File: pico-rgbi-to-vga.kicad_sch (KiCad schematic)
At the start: 25 parts, among them J1 SDS-80J, J2 DB15_Female_HighDensity, J3 USB-B1HSB6, SW1 SW_Push, U1 Pico

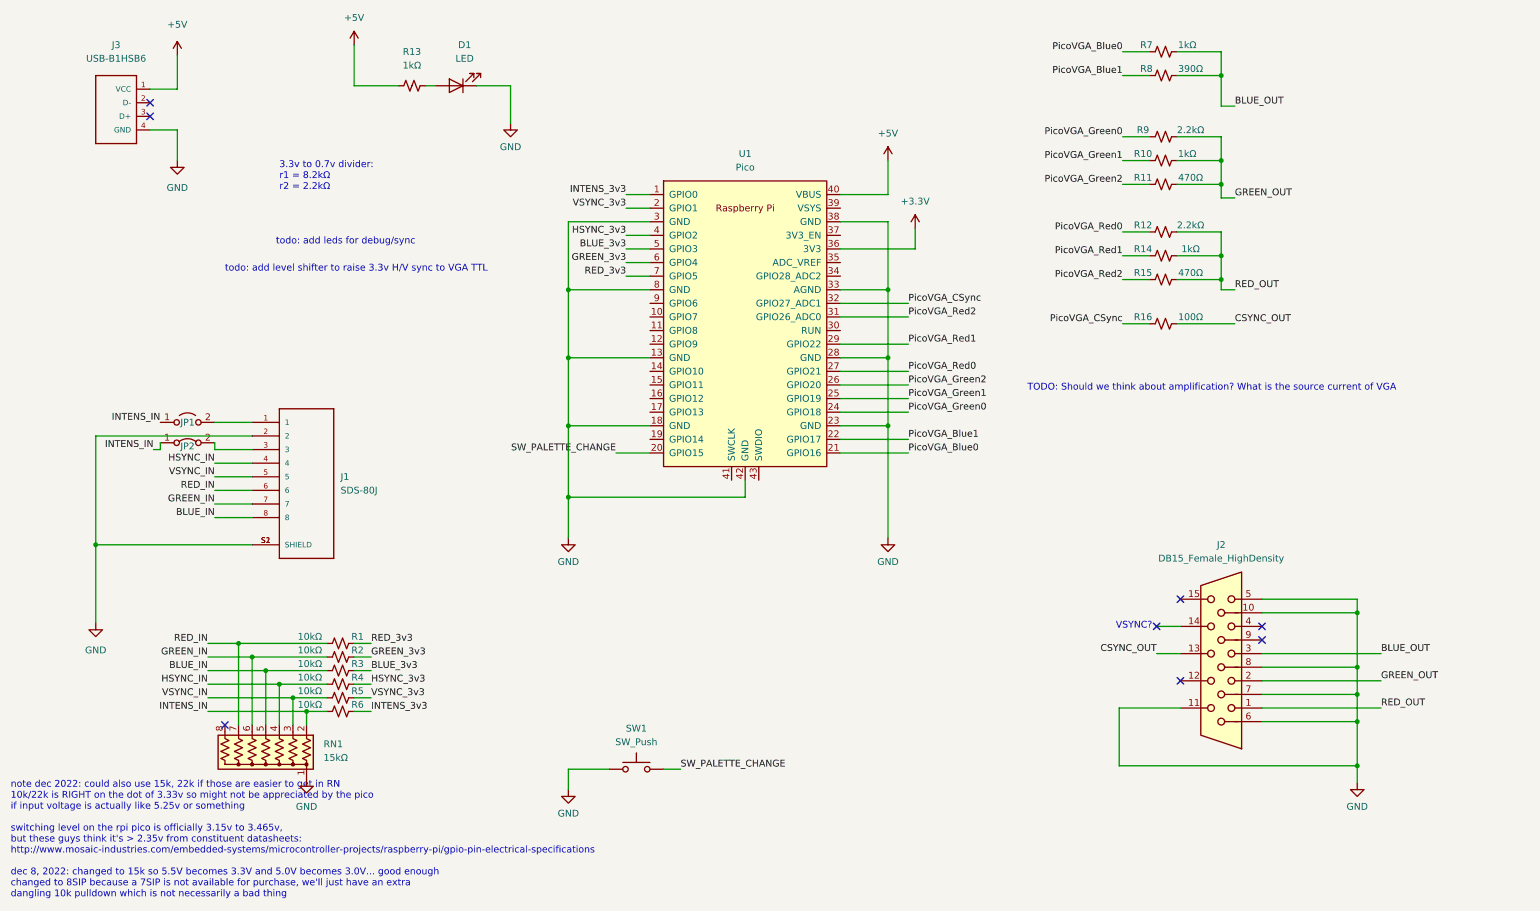
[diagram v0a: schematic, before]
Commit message: Fix VGA output pins to use GPIOs that exist
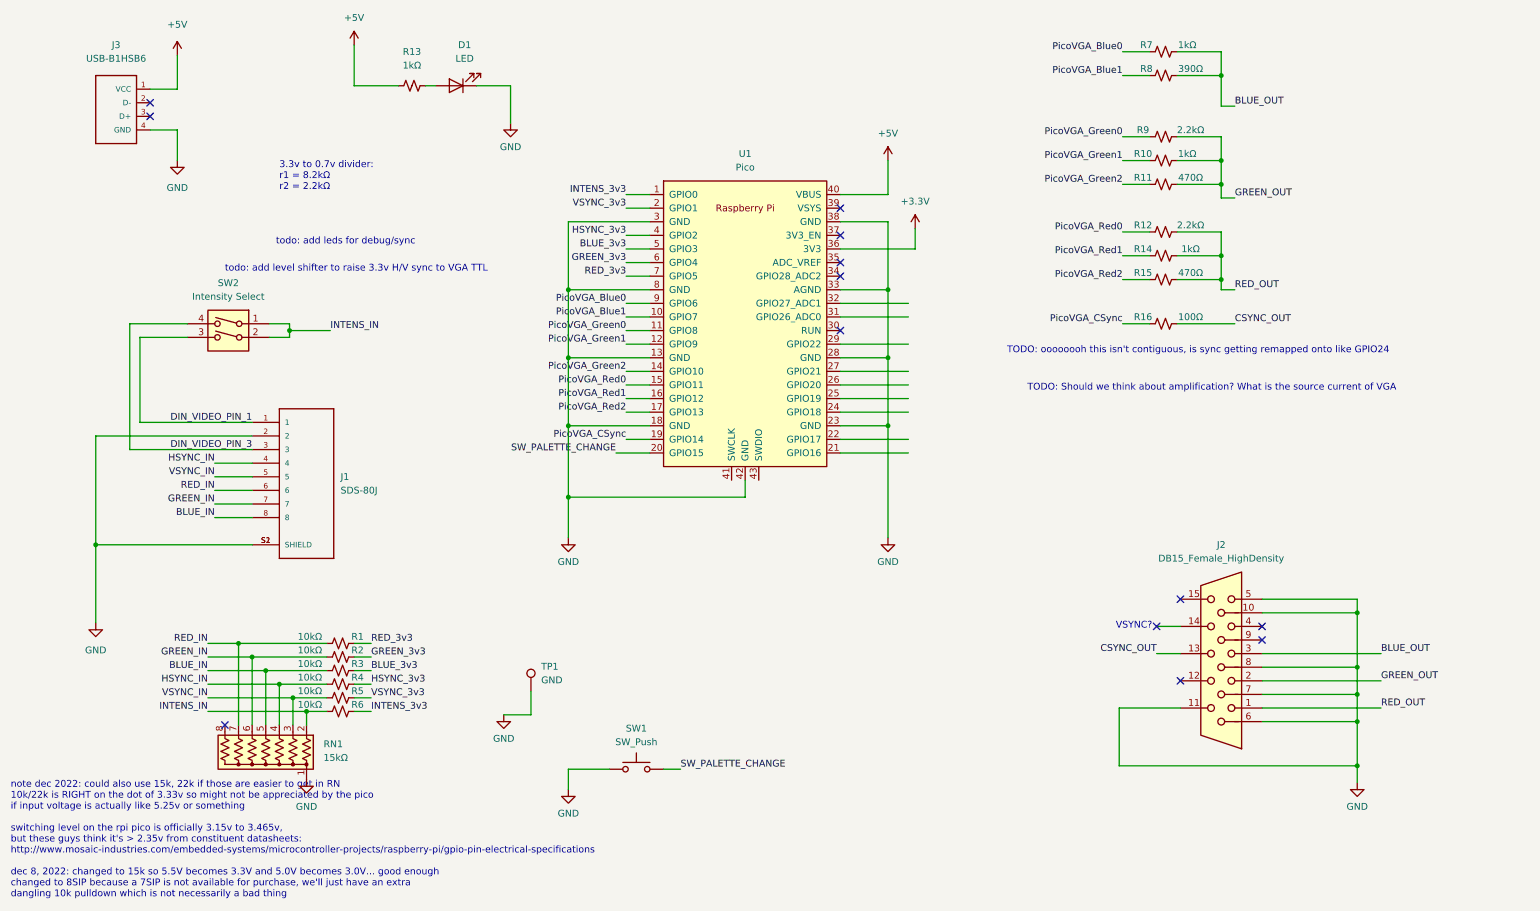
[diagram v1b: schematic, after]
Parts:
- removed JP1: Jumper_2_Open, Jumper:SolderJumper-2_P1.3mm_Open_RoundedPad1.0x1.5mm, symbol Jumper:Jumper_2_Open
- removed JP2: Jumper_2_Bridged, Jumper:SolderJumper-2_P1.3mm_Bridged_RoundedPad1.0x1.5mm, symbol Jumper:Jumper_2_Bridged
- added SW2: Intensity Select, Button_Switch_THT:SW_DIP_SPSTx02_Slide_6.7x6.64mm_W7.62mm_P2.54mm_LowProfile, symbol Switch:SW_DIP_x02
- added TP1: GND, TestPoint:TestPoint_Loop_D2.54mm_Drill1.5mm_Beaded, symbol Connector:TestPoint
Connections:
- net GND: now also TP1.1
- net INTENS_IN: now also SW2.1, SW2.2
- net PicoVGA_Blue0: now also U1.9 (GPIO6); no longer U1.21 (GPIO16)
- net PicoVGA_Blue1: now also U1.10 (GPIO7); no longer U1.22 (GPIO17)
- net PicoVGA_CSync: now also U1.19 (GPIO14); no longer U1.32 (GPIO27_ADC1)
- net PicoVGA_Green0: now also U1.11 (GPIO8); no longer U1.24 (GPIO18)
- net PicoVGA_Green1: now also U1.12 (GPIO9); no longer U1.25 (GPIO19)
- net PicoVGA_Green2: now also U1.14 (GPIO10); no longer U1.26 (GPIO20)
- net PicoVGA_Red0: now also U1.15 (GPIO11); no longer U1.27 (GPIO21)
- net PicoVGA_Red1: now also U1.16 (GPIO12); no longer U1.29 (GPIO22)
- net PicoVGA_Red2: now also U1.17 (GPIO13); no longer U1.31 (GPIO26_ADC0)
- net DIN_VIDEO_PIN_3: now reaches J1.3
- net DIN_VIDEO_PIN_3: now also SW2.4
- net DIN_VIDEO_PIN_1: now reaches J1.1
- net DIN_VIDEO_PIN_1: now also SW2.3
- no-connect marks 8 -> 13
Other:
- note added: "TODO: oooooooh this isn't contiguous, is sync getting remapped onto like GPIO24"

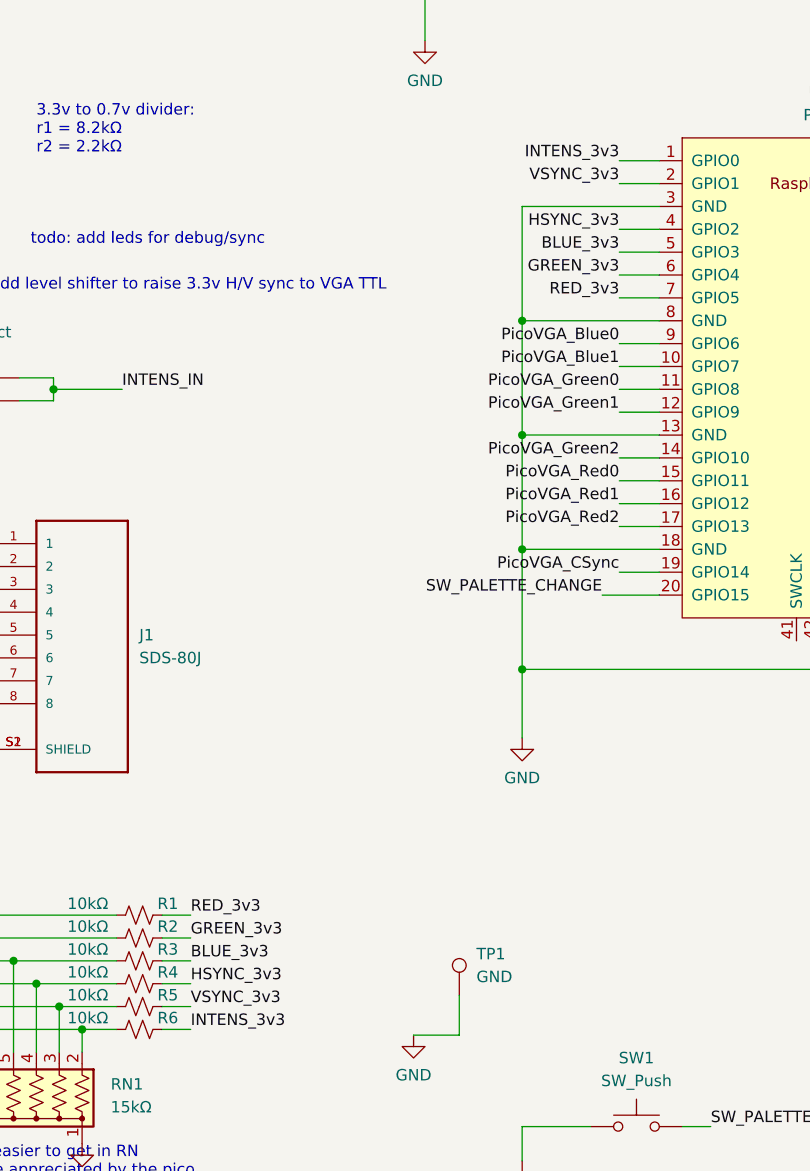
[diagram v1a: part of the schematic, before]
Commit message: KiCad7; reorder pins so HV won't get captured
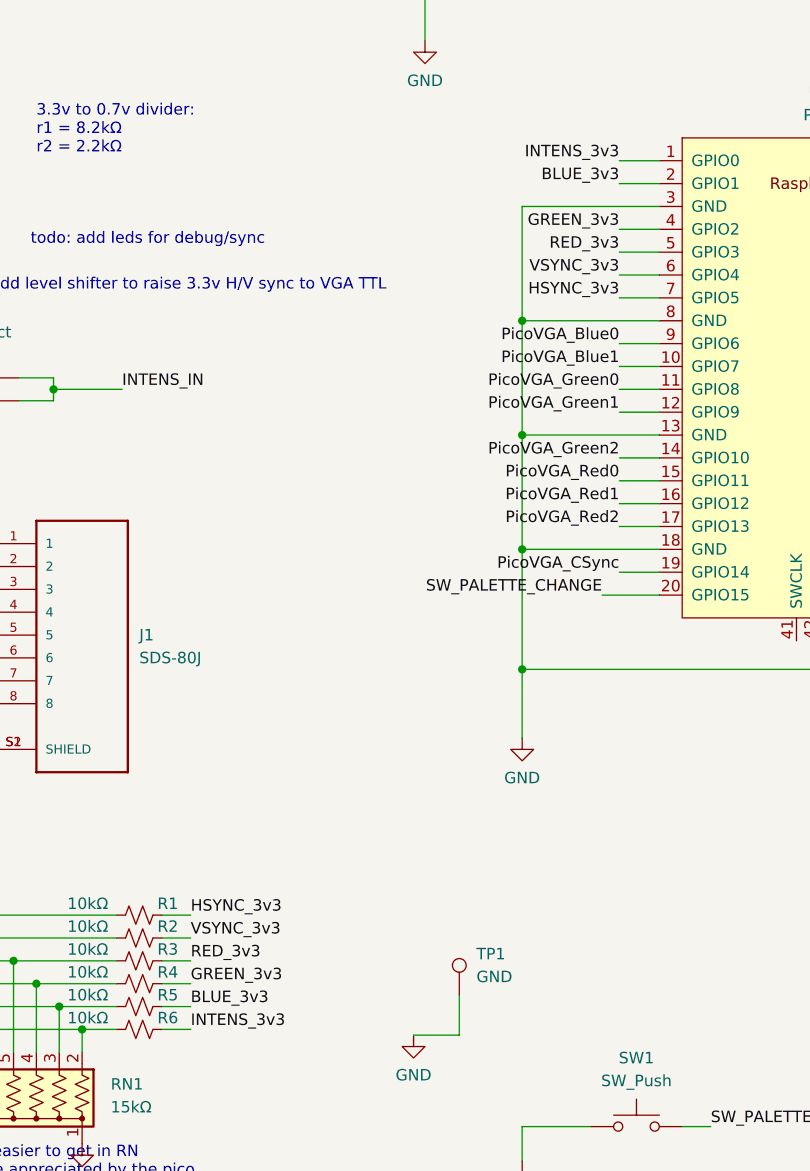
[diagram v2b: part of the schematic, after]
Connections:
- net BLUE_3v3: now also R5.1, U1.2 (GPIO1); no longer R3.1, U1.5 (GPIO3)
- net GREEN_3v3: now also R4.1, U1.4 (GPIO2); no longer R2.1, U1.6 (GPIO4)
- net HSYNC_3v3: now also R1.1, U1.7 (GPIO5); no longer R4.1, U1.4 (GPIO2)
- net RED_3v3: now also R3.1, U1.5 (GPIO3); no longer R1.1, U1.7 (GPIO5)
- net VSYNC_3v3: now also R2.1, U1.6 (GPIO4); no longer R5.1, U1.2 (GPIO1)

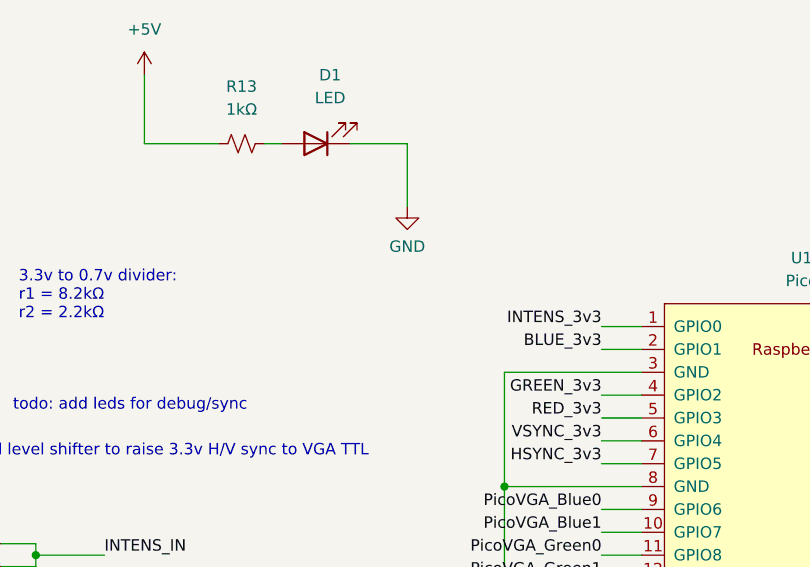
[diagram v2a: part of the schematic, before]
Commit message: Rewired to be IBGRHV
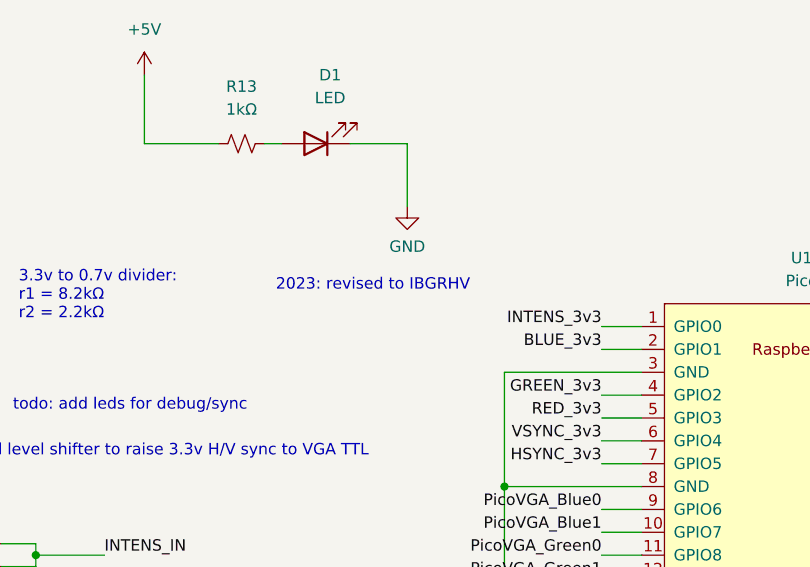
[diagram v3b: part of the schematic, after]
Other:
- note added: "2023: revised to IBGRHV"
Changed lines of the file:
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@@
+    (effects (font (size 1.27 1.27)) (justify left bottom))
+  )
+  (text "2023: revised to IBGRHV" (at 95.25 43.18 0)
     (effects (font (size 1.27 1.27)) (justify left bottom))
   )

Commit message: Doubts about DIN8 pinout
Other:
- note added: "todo: is this backward?"
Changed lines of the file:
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@@
+    (effects (font (size 1.27 1.27)) (justify left bottom))
+  )
+  (text "todo: is this backward?" (at 53.34 85.725 0)
     (effects (font (size 1.27 1.27)) (justify left bottom))
   )

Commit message: Set heights for turbocase
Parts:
- J1: Height (none) -> 22
- J2: Height (none) -> 12.88
- J3: Height (none) -> 10.9
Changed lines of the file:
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@@
       (effects (font (size 1.27 1.27)) (justify left bottom) hide)
+    )
+    (property "Height" "22" (at 71.755 99.695 0)
+      (effects (font (size 1.27 1.27)) hide)
     )
     (pin "1")
@@
       (effects (font (size 1.27 1.27)) hide)
     )
+    (property "Height" "10.9" (at 40.005 29.845 0)
+      (effects (font (size 1.27 1.27)) hide)
+    )
     (pin "1")
     (pin "2")
@@
       (effects (font (size 1.27 1.27)) hide)
     )
+    (property "Height" "12.88" (at 242.57 132.715 0)
+      (effects (font (size 1.27 1.27)) hide)
+    )

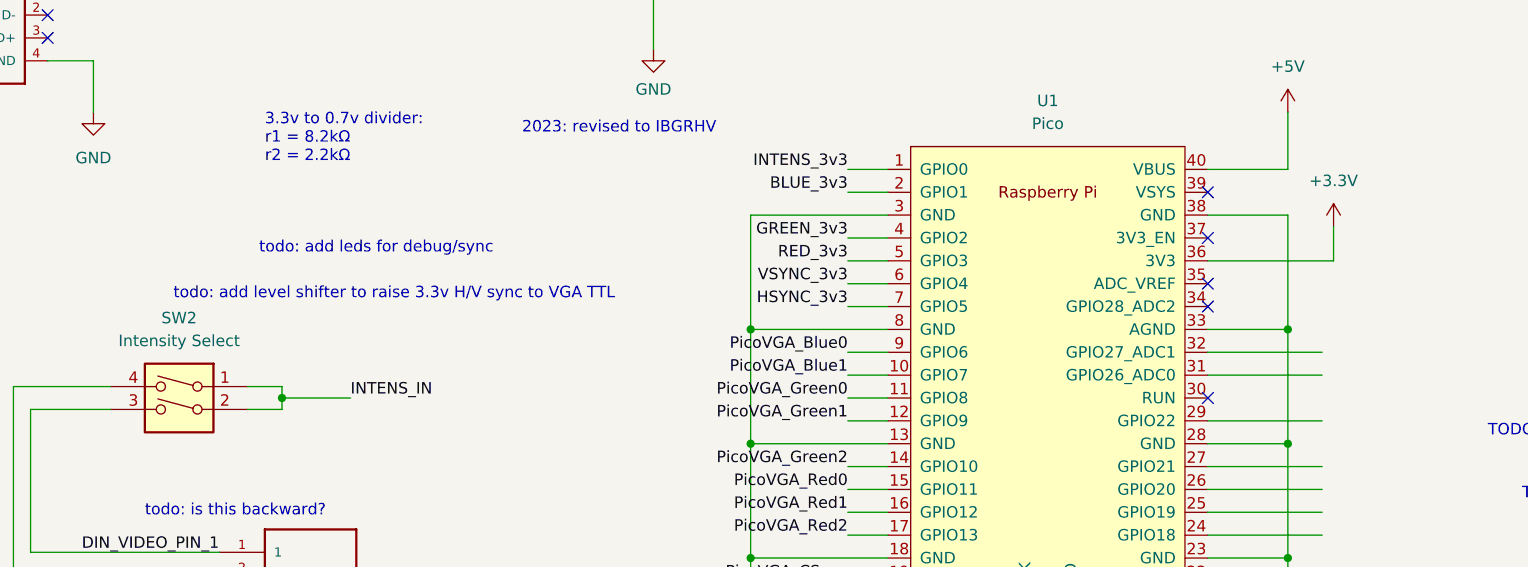
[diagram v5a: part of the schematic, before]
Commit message: Update to kicad 8
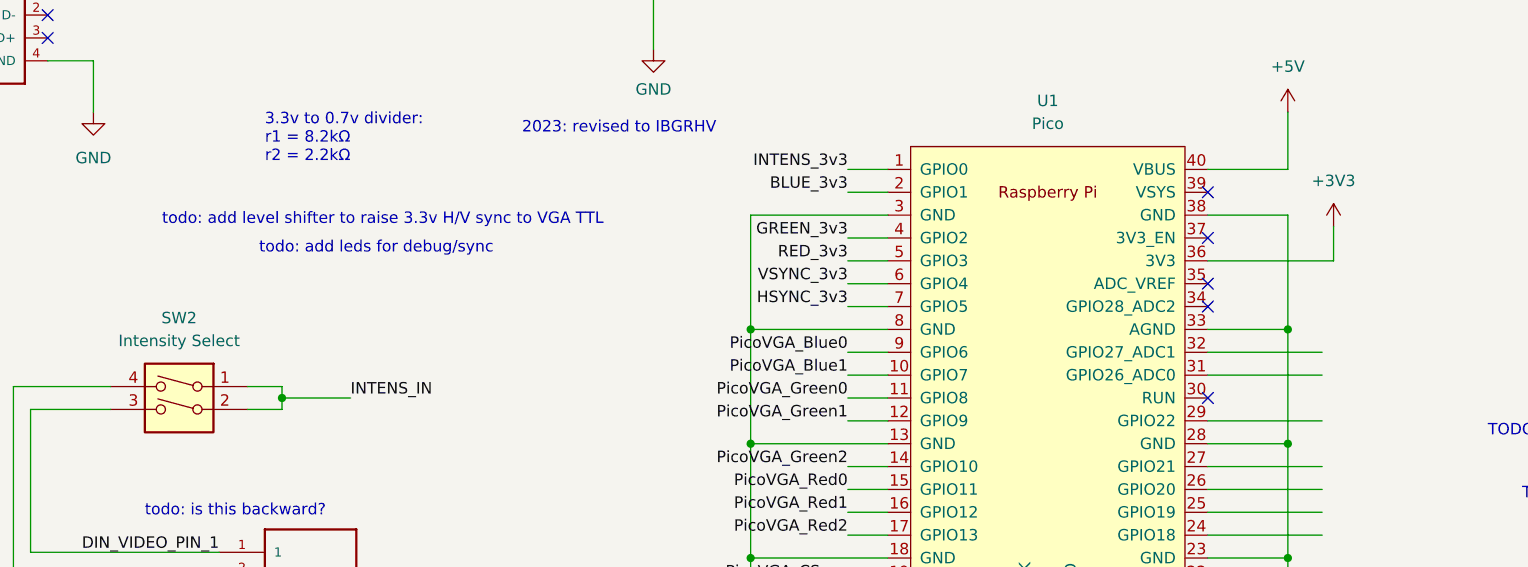
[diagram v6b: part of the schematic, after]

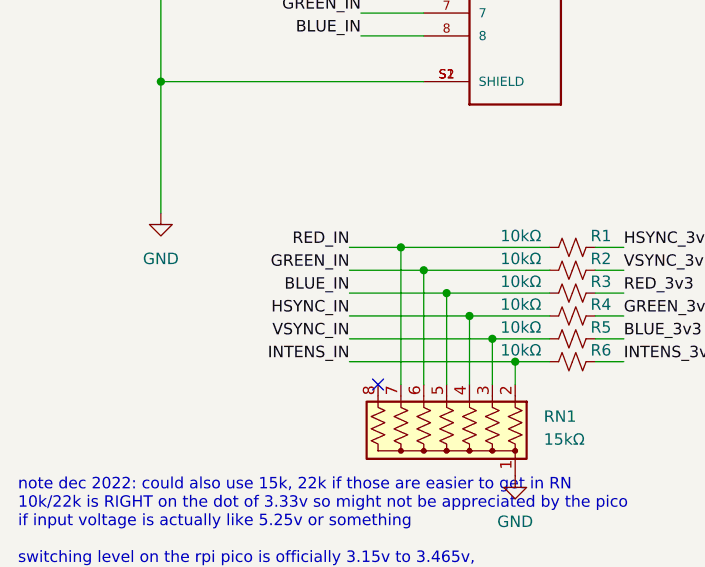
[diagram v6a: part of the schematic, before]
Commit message: Fix boneheaded pinout mixup
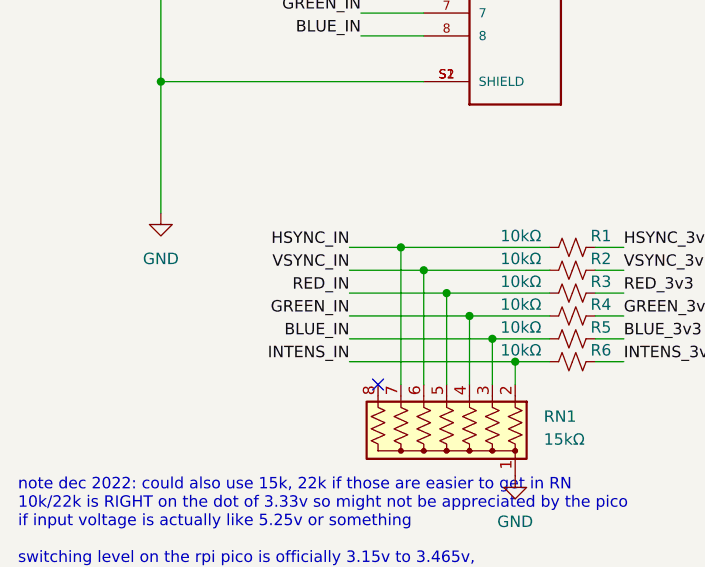
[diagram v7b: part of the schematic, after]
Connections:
- net BLUE_IN: now also R5.2, RN1.3 (R2); no longer R3.2, RN1.5 (R4)
- net GREEN_IN: now also R4.2, RN1.4 (R3); no longer R2.2, RN1.6 (R5)
- net HSYNC_IN: now also R1.2, RN1.7 (R6); no longer R4.2, RN1.4 (R3)
- net RED_IN: now also R3.2, RN1.5 (R4); no longer R1.2, RN1.7 (R6)
- net VSYNC_IN: now also R2.2, RN1.6 (R5); no longer R5.2, RN1.3 (R2)
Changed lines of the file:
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@@
 	)
 	(label "HSYNC_IN"
-		(at 53.34 138.43 180)
+		(at 53.34 130.81 180)
 		(fields_autoplaced yes)
 		(effects
@@
 	)
 	(label "GREEN_IN"
-		(at 53.34 133.35 180)
+		(at 53.34 138.43 180)
 		(fields_autoplaced yes)
 		(effects
@@
 	)
 	(label "VSYNC_IN"
-		(at 53.34 140.97 180)
+		(at 53.34 133.35 180)
 		(fields_autoplaced yes)
 		(effects
@@
 	)
 	(label "RED_IN"
-		(at 53.34 130.81 180)
+		(at 53.34 135.89 180)
 		(fields_autoplaced yes)
 		(effects
@@
 	)
 	(label "BLUE_IN"
-		(at 53.34 135.89 180)
-		(fields_autoplaced yes)
-		(effects
+		(at 53.34 140.97 180)
+		(fields_autoplaced yes)
+		(effects
